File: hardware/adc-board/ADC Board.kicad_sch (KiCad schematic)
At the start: 60 parts, among them J10 BootJumper, J11 USB Header, J2 ST-LINK/V2, J3 USART3, J4 USART1, J5 UE27AC5410H, J7 AltPowerInput, J8 USBPowerJumper, J9 USART2, U0 STM32H743ZITx, U13 3.3V Reg, U7 MCP120-xxxxTT, U9 USBLC6-2SC6

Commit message: Unified ground nets in schematic and layout.
* Rearranged the layers that pours are on.
* Added the keep-out zone separating analog and
  digital areas from each other.
* Tightened up placement of decoupling capacitors.
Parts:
- removed JP0: SolderJumper_2_Bridged, Jumper:SolderJumper-2_P1.3mm_Bridged_RoundedPad1.0x1.5mm, symbol Jumper:SolderJumper_2_Bridged
- removed U7: MCP120-xxxxTT, TO_SOT_Packages_SMD:SOT-23, symbol Power_Supervisor:MCP120-xxxxTT
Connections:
- net GNDD is gone; now on net GND: C1.2, C33.2, C34.2, C35.2, C36.2, C37.2, C38.2, C39.2, C40.2, C41.2, C42.2, C43.2, C44.2, C45.2, C46.2, C47.2, C48.2, C53.2, C54.2, C55.2, C56.2, H1.1, H2.1, H3.1, H4.1, J11.1 (Pin_1), J2.10 (Pin_10), J2.12 (Pin_12), J2.14 (Pin_14), J2.16 (Pin_16), J2.18 (Pin_18), J2.20 (Pin_20), J2.4 (Pin_4), J2.6 (Pin_6), J2.8 (Pin_8), J3.3 (Pin_3), J4.3 (Pin_3), J5.4 (GND), J5.5 (Shield), J7.2 (Pin_2), J9.3 (Pin_3), R24.2, R25.2, R30.2, R55.2, R56.2, R57.2, R58.2, U0.107 (VSS), U0.120 (VSS), U0.130 (VSS), U0.16 (VSS), U0.38 (VSS), U0.51 (VSS), U0.61 (VSS), U0.83 (VSS), U0.94 (VSS), U13.2 (GND), U9.2 (GND)
- net GNDA renamed GND
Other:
- note removed: "Represents single connection between GNDD and GNDA near the 5V regulator. Could be cut and choke inserted."

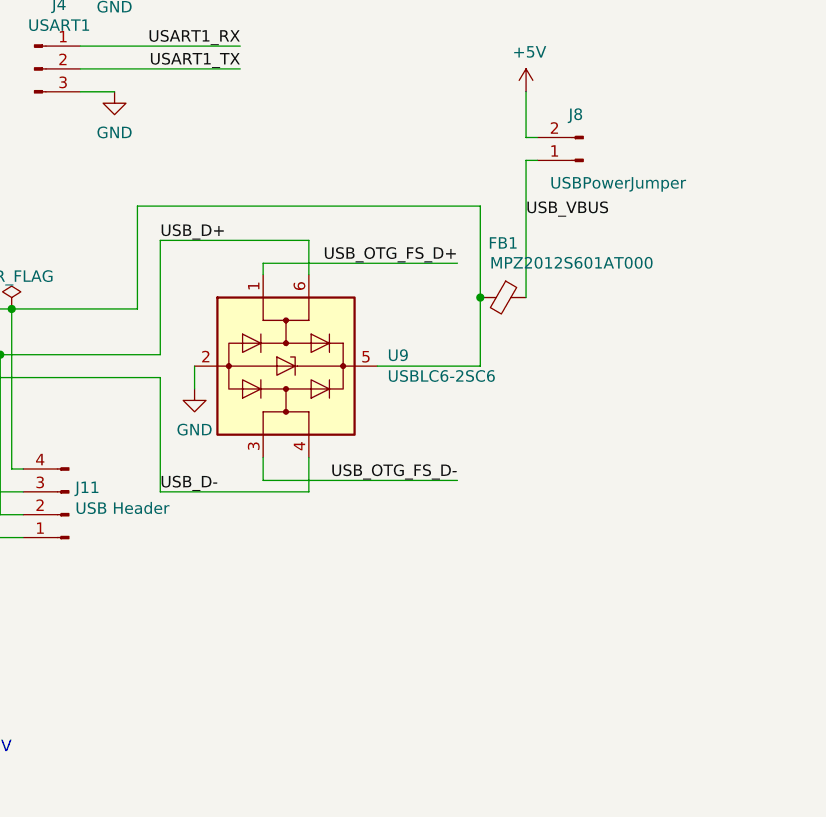
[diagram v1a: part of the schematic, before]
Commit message: More ADC board rev 3 changes, per issue #47
* 4.5V regulator for phototransistors
* new 3.3V regulator for analog section
* new 2.0V precision voltage reference
* Analog voltages and their distribution rearranged
* Tidied up traces on the left hand side, everything is nice and curvy now
* Adjusted USB ESD protection to be optional and/or support other parts
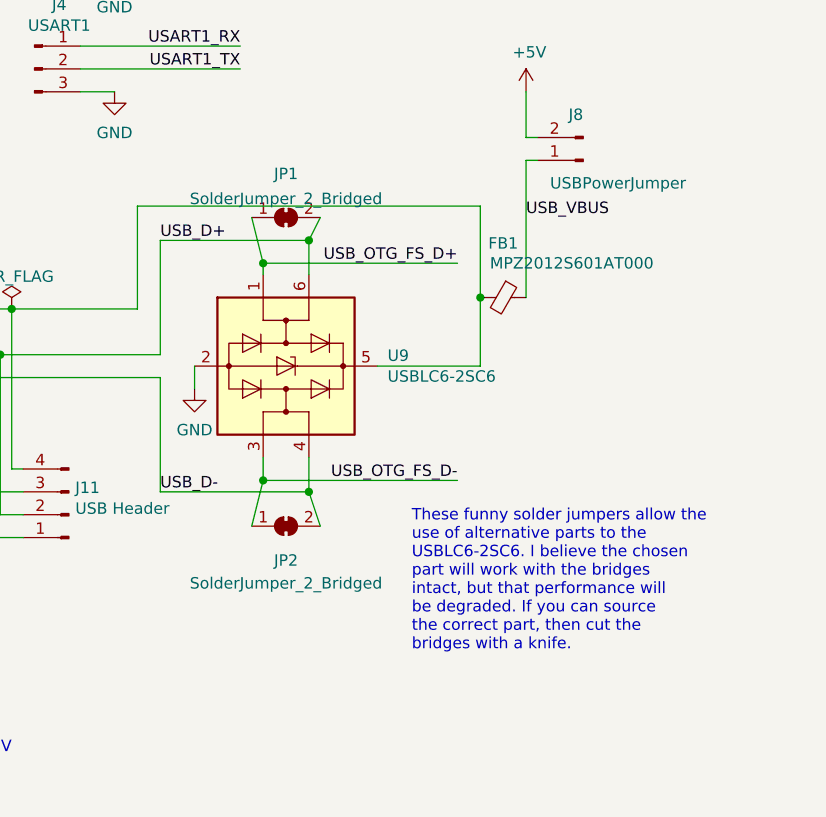
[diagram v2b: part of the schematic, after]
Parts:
- added JP1, JP2: SolderJumper_2_Bridged, Jumper:SolderJumper-2_P1.3mm_Bridged_RoundedPad1.0x1.5mm, symbol Jumper:SolderJumper_2_Bridged
- C1, C32, C33, C34, C35, C36, C37, C38, C39, C40, C41, C42, C43, C44, C45, C46, C47, C48, C55, C56: footprint Capacitors_SMD:C_0805 -> Capacitor_SMD:C_0805_2012Metric
- C53: footprint Capacitors_SMD:CP_Elec_5x5.3 -> Capacitor_SMD:CP_Elec_5x5.3
- C54: footprint Capacitors_SMD:CP_Elec_6.3x5.3 -> Capacitor_SMD:CP_Elec_6.3x5.3
- D1, D2, D3, D4, D5: footprint LEDs:LED_0805_HandSoldering -> LED_SMD:LED_0805_2012Metric_Pad1.15x1.40mm_HandSolder
- FB1: footprint Inductors_SMD:L_0805 -> Inductor_SMD:L_0805_2012Metric_Pad1.05x1.20mm_HandSolder
- H1, H2, H3, H4: footprint Mounting_Holes:MountingHole_3.2mm_M3_Pad_Via -> MountingHole:MountingHole_3.2mm_M3_Pad_Via
- R23, R24, R25, R30, R55, R56, R57, R58: footprint Resistors_SMD:R_0805 -> Resistor_SMD:R_0805_2012Metric
- TP23, TP24, TP25, TP26, TP27, TP28: footprint Testpoint:TestPoint_Pad_D1.5mm -> TestPoint:TestPoint_Pad_D1.5mm
- U0: footprint Housings_QFP:LQFP-144_20x20mm_Pitch0.5mm -> Package_QFP:TQFP-144_20x20mm_P0.5mm
- U9: footprint TO_SOT_Packages_SMD:SOT-23-6_Handsoldering -> Package_TO_SOT_SMD:SOT-23-6_Handsoldering
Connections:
- net USB_D+: now also JP1.2 (B)
- net USB_D-: now also JP2.2 (B)
- net USB_OTG_FS_D+: now also JP1.1 (A)
- net USB_OTG_FS_D-: now also JP2.1 (A)
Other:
- note added: "These funny solder jumpers allow the use of alternative parts to the USBLC6-2SC6. I believe the chosen part will work with the bridges intact, but that performance will be degraded. If you can source the correct part, then cut the bridges with a knife."

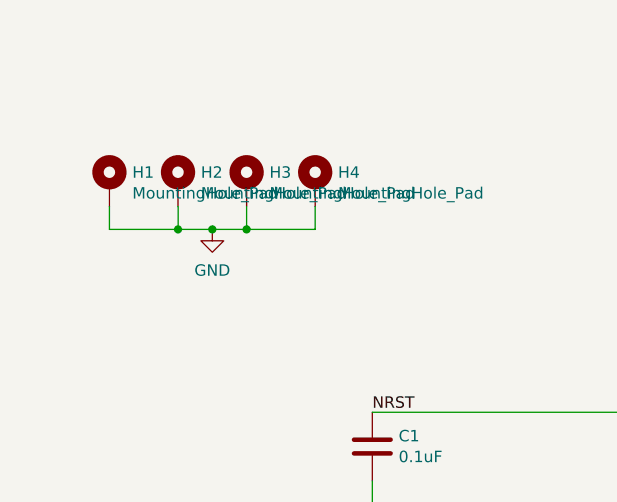
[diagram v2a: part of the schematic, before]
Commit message: ADC board layout tweaks; rearranged the various power planes
* Moved to standard plane layout of power, ground, ground, power,
  which I should've done from the start.
* Removed pads from the mounting holes, don't want to risk ground
  loops through the frame, there's no value.
* Adjusted the position of the 3.3VA regulator.
* Tweaked/tightened up a lot of traces, trying to keep them shorter.
* Bunch of extra vias stitching planes together.
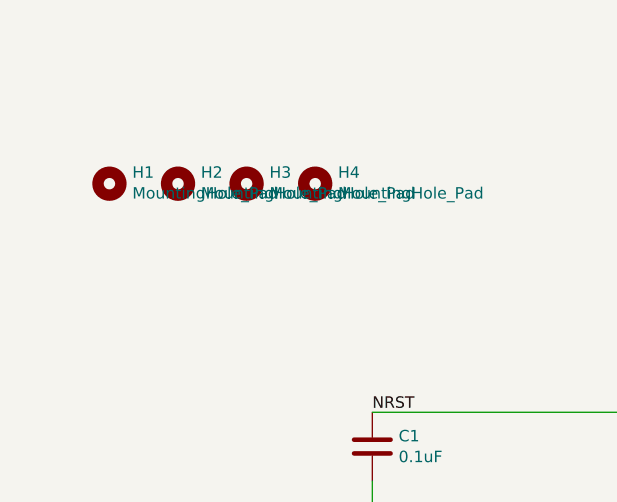
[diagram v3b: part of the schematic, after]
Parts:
- H1, H2, H3, H4: footprint MountingHole:MountingHole_3.2mm_M3_Pad_Via -> MountingHole:MountingHole_3.2mm_M3; symbol Mechanical:MountingHole_Pad -> Mechanical:MountingHole
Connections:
- net GND: no longer H1.1, H2.1, H3.1, H4.1
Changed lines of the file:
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@@
   (junction (at 295.91 129.54) (diameter 0) (color 0 0 0 0)
   )
-  (junction (at 36.83 39.37) (diameter 0) (color 0 0 0 0)
-  )
   (junction (at 336.55 31.75) (diameter 0) (color 0 0 0 0)
   )
@@
   (junction (at 364.49 121.92) (diameter 0) (color 0 0 0 0)
   )
-  (junction (at 40.64 39.37) (diameter 0) (color 0 0 0 0)
-  )
-  (junction (at 33.02 39.37) (diameter 0) (color 0 0 0 0)
-  )
   (junction (at 67.31 85.09) (diameter 0) (color 0 0 0 0)
   )
@@
   (no_connect (at 97.79 113.03))
   (no_connect (at 97.79 214.63))
-  (wire (pts (xy 40.64 36.83) (xy 40.64 39.37))
-    (stroke (width 0) (type default) (color 0 0 0 0))
-  )
   (wire (pts (xy 339.09 77.47) (xy 342.9 77.47))
     (stroke (width 0) (type default) (color 0 0 0 0))
@@
     (stroke (width 0) (type default) (color 0 0 0 0))
   )
-  (wire (pts (xy 40.64 39.37) (xy 48.26 39.37))
-    (stroke (width 0) (type default) (color 0 0 0 0))
-  )
   (wire (pts (xy 130.81 238.76) (xy 133.35 238.76))
     (stroke (width 0) (type default) (color 0 0 0 0))
@@
     (stroke (width 0) (type default) (color 0 0 0 0))
   )
-  (wire (pts (xy 33.02 39.37) (xy 36.83 39.37))
-    (stroke (width 0) (type default) (color 0 0 0 0))
-  )
   (wire (pts (xy 288.29 132.08) (xy 295.91 132.08))
     (stroke (width 0) (type default) (color 0 0 0 0))
@@
     (stroke (width 0) (type default) (color 0 0 0 0))
   )
-  (wire (pts (xy 33.02 39.37) (xy 25.4 39.37))
-    (stroke (width 0) (type default) (color 0 0 0 0))
-  )
   (wire (pts (xy 354.33 24.13) (xy 345.44 24.13))
     (stroke (width 0) (type default) (color 0 0 0 0))
@@
     (stroke (width 0) (type default) (color 0 0 0 0))
   )
-  (wire (pts (xy 25.4 36.83) (xy 25.4 39.37))
-    (stroke (width 0) (type default) (color 0 0 0 0))
-  )
   (wire (pts (xy 228.6 30.48) (xy 228.6 33.02))
     (stroke (width 0) (type default) (color 0 0 0 0))
@@
     (stroke (width 0) (type default) (color 0 0 0 0))
   )
-  (wire (pts (xy 36.83 39.37) (xy 40.64 39.37))
-    (stroke (width 0) (type default) (color 0 0 0 0))
-  )
   (wire (pts (xy 351.79 138.43) (xy 351.79 135.89))
     (stroke (width 0) (type default) (color 0 0 0 0))
@@
     (stroke (width 0) (type default) (color 0 0 0 0))
   )
-  (wire (pts (xy 33.02 36.83) (xy 33.02 39.37))
-    (stroke (width 0) (type default) (color 0 0 0 0))
-  )
   (wire (pts (xy 97.79 189.23) (xy 82.55 189.23))
     (stroke (width 0) (type default) (color 0 0 0 0))
@@
     (stroke (width 0) (type default) (color 0 0 0 0))
   )
-  (wire (pts (xy 48.26 39.37) (xy 48.26 36.83))
-    (stroke (width 0) (type default) (color 0 0 0 0))
-  )
   (wire (pts (xy 161.29 64.77) (xy 179.07 64.77))
     (stroke (width 0) (type default) (color 0 0 0 0))
@@
     (pin "3")
   )
-  (symbol (lib_id "Mechanical:MountingHole_Pad") (at 25.4 34.29 0) (unit 1)
+  (symbol (lib_id "Mechanical:MountingHole") (at 25.4 34.29 0) (unit 1)
     (in_bom yes) (on_board yes)
     (property "Reference" "H1" (id 0) (at 27.94 33.0454 0)
@@
       (effects (font (size 1.27 1.27)) (justify left))
     )
-    (property "Footprint" "MountingHole:MountingHole_3.2mm_M3_Pad_Via" (id 2) (at 25.4 34.29 0)
+    (property "Footprint" "MountingHole:MountingHole_3.2mm_M3" (id 2) (at 25.4 34.29 0)
       (effects (font (size 1.27 1.27)) hide)
     )
@@
       (effects (font (size 1.27 1.27)) hide)
     )
-    (pin "1")
   )
-  (symbol (lib_id "Mechanical:MountingHole_Pad") (at 33.02 34.29 0) (unit 1)
+  (symbol (lib_id "Mechanical:MountingHole") (at 33.02 34.29 0) (unit 1)
     (in_bom yes) (on_board yes)
     (property "Reference" "H2" (id 0) (at 35.56 33.0454 0)
@@
       (effects (font (size 1.27 1.27)) (justify left))
     )
-    (property "Footprint" "MountingHole:MountingHole_3.2mm_M3_Pad_Via" (id 2) (at 33.02 34.29 0)
+    (property "Footprint" "MountingHole:MountingHole_3.2mm_M3" (id 2) (at 33.02 34.29 0)
       (effects (font (size 1.27 1.27)) hide)
     )
@@
       (effects (font (size 1.27 1.27)) hide)
     )
-    (pin "1")
   )
-  (symbol (lib_id "Mechanical:MountingHole_Pad") (at 40.64 34.29 0) (unit 1)
+  (symbol (lib_id "Mechanical:MountingHole") (at 40.64 34.29 0) (unit 1)
     (in_bom yes) (on_board yes)
     (property "Reference" "H3" (id 0) (at 43.18 33.0454 0)
@@
       (effects (font (size 1.27 1.27)) (justify left))
     )
-    (property "Footprint" "MountingHole:MountingHole_3.2mm_M3_Pad_Via" (id 2) (at 40.64 34.29 0)
+    (property "Footprint" "MountingHole:MountingHole_3.2mm_M3" (id 2) (at 40.64 34.29 0)
       (effects (font (size 1.27 1.27)) hide)
     )
@@
       (effects (font (size 1.27 1.27)) hide)
     )
-    (pin "1")
   )
-  (symbol (lib_id "Mechanical:MountingHole_Pad") (at 48.26 34.29 0) (unit 1)
+  (symbol (lib_id "Mechanical:MountingHole") (at 48.26 34.29 0) (unit 1)
     (in_bom yes) (on_board yes)
     (property "Reference" "H4" (id 0) (at 50.8 33.0454 0)
@@
       (effects (font (size 1.27 1.27)) (justify left))
     )
-    (property "Footprint" "MountingHole:MountingHole_3.2mm_M3_Pad_Via" (id 2) (at 48.26 34.29 0)
+    (property "Footprint" "MountingHole:MountingHole_3.2mm_M3" (id 2) (at 48.26 34.29 0)
       (effects (font (size 1.27 1.27)) hide)
     )
@@
       (effects (font (size 1.27 1.27)) hide)
     )
-    (pin "1")
   )
   (symbol (lib_id "Connector:Conn_01x03_Male") (at 334.01 88.9 0) (unit 1)
@@
     (pin "1")
   )
-  (symbol (lib_id "power:GND") (at 36.83 39.37 0) (unit 1)
-    (in_bom yes) (on_board yes) (fields_autoplaced)
-    (property "Reference" "#PWR0124" (id 0) (at 36.83 45.72 0)
-      (effects (font (size 1.27 1.27)) hide)
-    )
-    (property "Value" "GND" (id 1) (at 36.83 43.9325 0))
-    (property "Footprint" "" (id 2) (at 36.83 39.37 0)
-      (effects (font (size 1.27 1.27)) hide)
-    )
-    (property "Datasheet" "" (id 3) (at 36.83 39.37 0)
-      (effects (font (size 1.27 1.27)) hide)
-    )
-    (pin "1")
-  )
   (symbol (lib_id "power:PWR_FLAG") (at 331.47 129.54 0) (unit 1)
     (in_bom yes) (on_board yes) (fields_autoplaced)
@@
       (reference "#PWR0123") (unit 1) (value "+3.3V") (footprint "")
     )
-    (path "/d3bc2c31-f430-4ded-8c81-598aaf62a003"
-      (reference "#PWR0124") (unit 1) (value "GND") (footprint "")
-    )
     (path "/00000000-0000-0000-0000-00005fa7e425/681c1223-723c-4917-8691-5f55c58c8b40"
       (reference "#PWR0125") (unit 1) (value "GND") (footprint "")
@@
     )
     (path "/00000000-0000-0000-0000-00005ff241d9"
-      (reference "H1") (unit 1) (value "MountingHole_Pad") (footprint "MountingHole:MountingHole_3.2mm_M3_Pad_Via")
+      (reference "H1") (unit 1) (value "MountingHole_Pad") (footprint "MountingHole:MountingHole_3.2mm_M3")
     )
     (path "/00000000-0000-0000-0000-00005ff253e7"
-      (reference "H2") (unit 1) (value "MountingHole_Pad") (footprint "MountingHole:MountingHole_3.2mm_M3_Pad_Via")
+      (reference "H2") (unit 1) (value "MountingHole_Pad") (footprint "MountingHole:MountingHole_3.2mm_M3")
     )
     (path "/00000000-0000-0000-0000-00005ff263ba"
-      (reference "H3") (unit 1) (value "MountingHole_Pad") (footprint "MountingHole:MountingHole_3.2mm_M3_Pad_Via")
+      (reference "H3") (unit 1) (value "MountingHole_Pad") (footprint "MountingHole:MountingHole_3.2mm_M3")
     )
     (path "/00000000-0000-0000-0000-00005ff27900"
-      (reference "H4") (unit 1) (value "MountingHole_Pad") (footprint "MountingHole:MountingHole_3.2mm_M3_Pad_Via")
+      (reference "H4") (unit 1) (value "MountingHole_Pad") (footprint "MountingHole:MountingHole_3.2mm_M3")
     )
     (path "/00000000-0000-0000-0000-00005fa7e425/00000000-0000-0000-0000-00005fb3f5ce"
